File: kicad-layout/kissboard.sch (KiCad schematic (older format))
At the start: 27 parts, among them J1 Conn_01x04, K1 KEYSW, K10 KEYSW, K11 KEYSW, K12 KEYSW, K13 KEYSW, K14 KEYSW, K15 KEYSW, K16 KEYSW, K17 KEYSW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

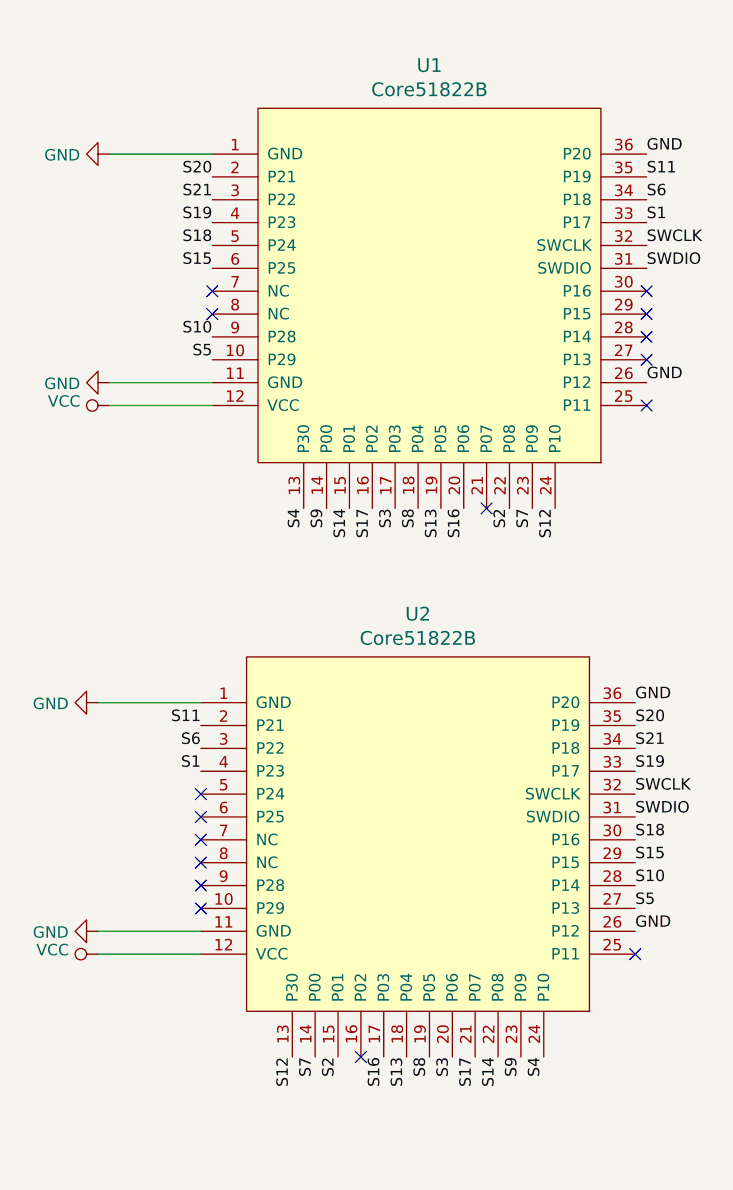
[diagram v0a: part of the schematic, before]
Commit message: traces complete, all files updated, gerber.zip added
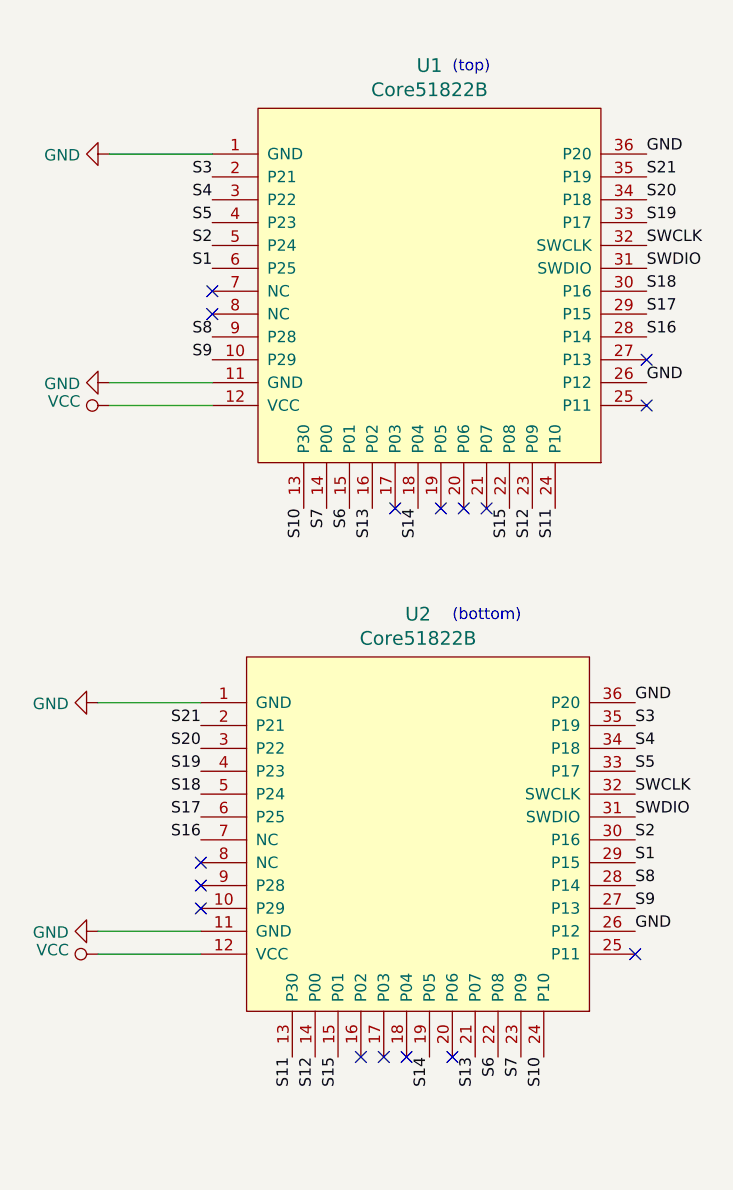
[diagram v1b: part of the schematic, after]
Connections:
- net S1: now also U1.6 (P25), U2.29 (P15); no longer U1.33 (P17), U2.4 (P23)
- net S10: now also U1.13 (P30), U2.24 (P10); no longer U1.9 (P28), U2.28 (P14)
- net S11: now also U1.24 (P10), U2.13 (P30); no longer U1.35 (P19), U2.2 (P21)
- net S12: now also U1.23 (P09), U2.14 (P00); no longer U1.24 (P10), U2.13 (P30)
- net S13: now also U1.16 (P02), U2.21 (P07); no longer U1.19 (P05), U2.18 (P04)
- net S14: now also U1.18 (P04), U2.19 (P05); no longer U1.15 (P01), U2.22 (P08)
- net S15: now also U1.22 (P08), U2.15 (P01); no longer U1.6 (P25), U2.29 (P15)
- net S16: now also U1.28 (P14), U2.7 (NC); no longer U1.20 (P06), U2.17 (P03)
- net S17: now also U1.29 (P15), U2.6 (P25); no longer U1.16 (P02), U2.21 (P07)
- net S18: now also U1.30 (P16), U2.5 (P24); no longer U1.5 (P24), U2.30 (P16)
- net S19: now also U1.33 (P17), U2.4 (P23); no longer U1.4 (P23), U2.33 (P17)
- net S2: now also U1.5 (P24), U2.30 (P16); no longer U1.22 (P08), U2.15 (P01)
- net S20: now also U1.34 (P18), U2.3 (P22); no longer U1.2 (P21), U2.35 (P19)
- net S21: now also U1.35 (P19), U2.2 (P21); no longer U1.3 (P22), U2.34 (P18)
- net S3: now also U1.2 (P21), U2.35 (P19); no longer U1.17 (P03), U2.20 (P06)
- net S4: now also U1.3 (P22), U2.34 (P18); no longer U1.13 (P30), U2.24 (P10)
- net S5: now also U1.4 (P23), U2.33 (P17); no longer U1.10 (P29), U2.27 (P13)
- net S6: now also U1.15 (P01), U2.22 (P08); no longer U1.34 (P18), U2.3 (P22)
- net S7: now also U1.14 (P00), U2.23 (P09); no longer U1.23 (P09), U2.14 (P00)
- net S8: now also U1.9 (P28), U2.28 (P14); no longer U1.18 (P04), U2.19 (P05)
- net S9: now also U1.10 (P29), U2.27 (P13); no longer U1.14 (P00), U2.23 (P09)
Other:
- note added: "(bottom)"
- note added: "(top)"
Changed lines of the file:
@@
 $EndComp
 Text Label 9550 2900 3    50   ~ 0
+S7
+Text Label 9650 2900 3    50   ~ 0
+S6
+Text Label 9750 2900 3    50   ~ 0
+S13
+Text Label 9950 2900 3    50   ~ 0
+S14
+Text Label 10350 2900 3    50   ~ 0
+S15
+Text Label 10450 2900 3    50   ~ 0
+S12
+Text Label 10550 2900 3    50   ~ 0
+S11
+Text Label 9050 1450 2    50   ~ 0
+S3
+Text Label 9050 2150 2    50   ~ 0
+S8
+Text Label 9050 2250 2    50   ~ 0
 S9
-Text Label 9650 2900 3    50   ~ 0
-S14
-Text Label 9750 2900 3    50   ~ 0
-S17
-Text Label 9850 2900 3    50   ~ 0
-S3
-Text Label 9950 2900 3    50   ~ 0
-S8
-Text Label 10050 2900 3    50   ~ 0
-S13
-Text Label 10150 2900 3    50   ~ 0
-S16
-Text Label 10550 2900 3    50   ~ 0
-S12
-Text Label 10450 2900 3    50   ~ 0
-S7
-Text Label 10350 2900 3    50   ~ 0
-S2
-Text Label 9050 1450 2    50   ~ 0
-S20
-Text Label 9050 2150 2    50   ~ 0
-S10
-Text Label 9050 2250 2    50   ~ 0
-S5
 $Comp
 L power:GND #PWR0101
@@
 NoConn ~ 10950 2450
 Text Label 9450 2900 3    50   ~ 0
-S4
+S10
 $Comp
 L core51822b:Core51822B U2
@@
 	1    0    0    -1
 $EndComp
-Text Label 9800 5300 3    50   ~ 0
-S16
-Text Label 9900 5300 3    50   ~ 0
-S13
-Text Label 10000 5300 3    50   ~ 0
-S8
-Text Label 10100 5300 3    50   ~ 0
-S3
-Text Label 10200 5300 3    50   ~ 0
-S17
-Text Label 10300 5300 3    50   ~ 0
-S14
-Text Label 10400 5300 3    50   ~ 0
-S9
-Text Label 10500 5300 3    50   ~ 0
-S4
-Text Label 10900 4650 0    50   ~ 0
-S5
-Text Label 10900 4550 0    50   ~ 0
-S10
-Text Label 10900 4450 0    50   ~ 0
-S15
 Text Label 9400 5300 3    50   ~ 0
+S11
+Text Label 9500 5300 3    50   ~ 0
 S12
 Text Label 9600 5300 3    50   ~ 0
-S2
+S15
+Text Label 10000 5300 3    50   ~ 0
+S14
+Text Label 10200 5300 3    50   ~ 0
+S13
+Text Label 10300 5300 3    50   ~ 0
+S6
+Text Label 10400 5300 3    50   ~ 0
+S7
+Text Label 10500 5300 3    50   ~ 0
+S10
+Text Label 10900 4650 0    50   ~ 0
+S9
+Text Label 10900 4550 0    50   ~ 0
+S8
+Text Label 10900 4450 0    50   ~ 0
+S1
 $Comp
 L power:GND #PWR0105
@@
 SWCLK
 Text Label 10900 3850 0    50   ~ 0
-S20
+S3
 Text Label 10900 3750 0    50   ~ 0
 GND
 Text Label 10900 4750 0    50   ~ 0
 GND
-Text Label 9500 5300 3    50   ~ 0
-S7
 NoConn ~ 9000 4450
 Text Label 10950 1350 0    50   ~ 0
@@
 	5000 3150 4850 3150
 Text Label 9000 3850 2    50   ~ 0
-S11
+S21
 Text Label 9000 3950 2    50   ~ 0
-S6
+S20
 Text Label 9000 4050 2    50   ~ 0
-S1
+S19
 Text Label 10950 1450 0    50   ~ 0
-S11
+S21
 Text Label 10950 1550 0    50   ~ 0
-S6
+S20
 Text Label 10950 1650 0    50   ~ 0
-S1
-NoConn ~ 9000 4350
+S19
 Text Label 10900 3950 0    50   ~ 0
-S21
+S4
 Text Label 10900 4050 0    50   ~ 0
-S19
+S5
 Text Label 9050 1550 2    50   ~ 0
-S21
+S4
 Text Label 9050 1650 2    50   ~ 0
-S19
+S5
 Text Label 10900 4350 0    50   ~ 0
-S18
+S2
 NoConn ~ 10900 4850
 Text Label 9050 1750 2    50   ~ 0
-S18
+S2
 Text Label 9050 1850 2    50   ~ 0
-S15
+S1
 NoConn ~ 10950 2250
 NoConn ~ 10250 2900
@@
 NoConn ~ 9000 4650
 NoConn ~ 9000 4550
-NoConn ~ 10950 2150
-NoConn ~ 9000 4150
-NoConn ~ 9000 4250
-NoConn ~ 10950 2050
-NoConn ~ 10950 1950
+Text Notes 10100 3400 0    50   ~ 0
+(bottom)
+Text Notes 10100 1000 0    50   ~ 0
+(top)
+Text Label 9000 4150 2    50   ~ 0
+S18
+Text Label 9000 4250 2    50   ~ 0
+S17
+Text Label 9000 4350 2    50   ~ 0
+S16
+Text Label 10950 1950 0    50   ~ 0
+S18
+Text Label 10950 2050 0    50   ~ 0
+S17
+Text Label 10950 2150 0    50   ~ 0
+S16
+NoConn ~ 9800 5300
+NoConn ~ 9900 5300
+NoConn ~ 10100 5300
+NoConn ~ 9850 2900
+NoConn ~ 10050 2900
+NoConn ~ 10150 2900
 $EndSCHEMATC

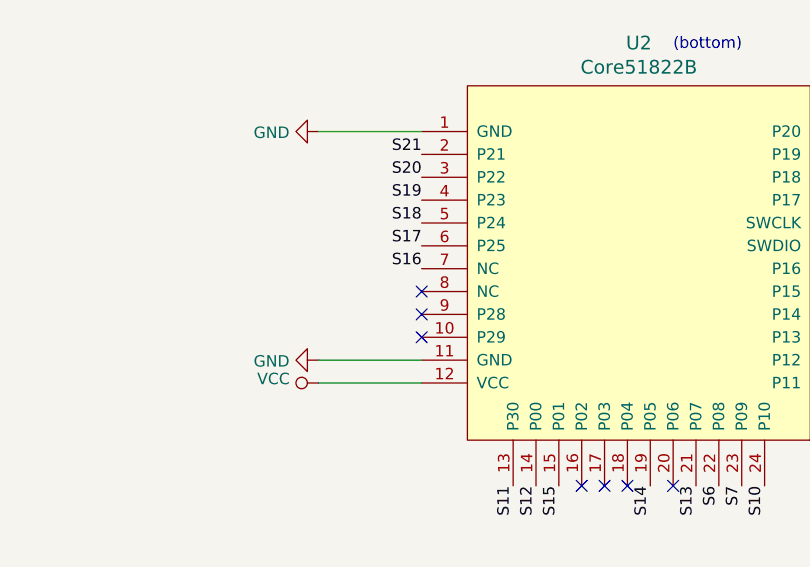
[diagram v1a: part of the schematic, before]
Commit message: Fixed wrong connection of S16 on the bottom layer
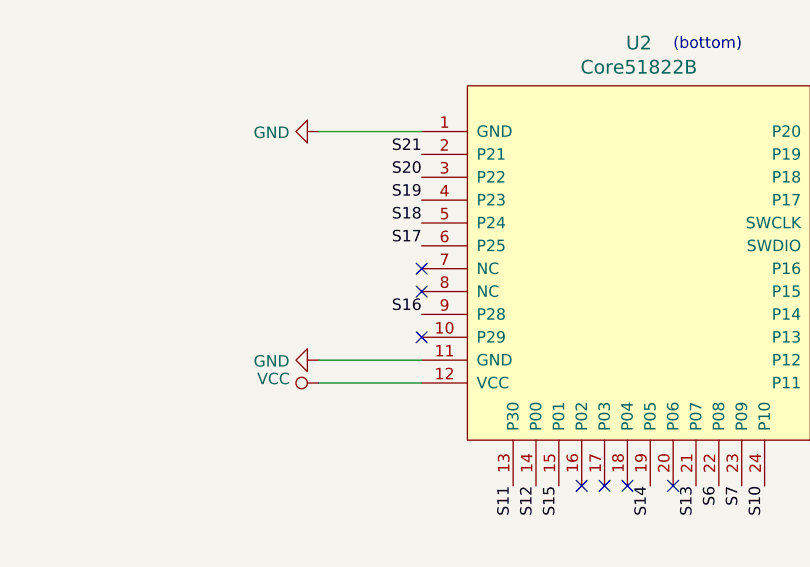
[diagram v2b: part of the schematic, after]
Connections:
- net S16: now also U2.9 (P28); no longer U2.7 (NC)
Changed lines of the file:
@@
 NoConn ~ 9700 5300
 NoConn ~ 9000 4650
-NoConn ~ 9000 4550
+NoConn ~ 9000 4350
 Text Notes 10100 3400 0    50   ~ 0
 (bottom)
@@
 Text Label 9000 4250 2    50   ~ 0
 S17
-Text Label 9000 4350 2    50   ~ 0
+Text Label 9000 4550 2    50   ~ 0
 S16
 Text Label 10950 1950 0    50   ~ 0
